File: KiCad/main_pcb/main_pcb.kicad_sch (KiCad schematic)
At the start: 5 parts

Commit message: feat(KiCad): Adds circuit for the screens
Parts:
- removed U1, U5: (no value), symbol Lily's_Pad:Logic_Converter
- added C1: (no value), symbol Lily's_Pad:Capacitor
- added J1: (no value), symbol Lily's_Pad:Header_21
- added R1: (no value), symbol Lily's_Pad:Resistor
- added S1: (no value), symbol Lily's_Pad:Push-button_Switch
- added U1: (no value), symbol Lily's_Pad:ATmega_2560
- added U5, U7: TI TXB0104DR, symbol Lily's_Pad:TI TXB0104DR
- added U8: CH340C, symbol Lily's_Pad:CH340C
- added Y1: (no value), symbol Lily's_Pad:Crystal
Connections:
- net EYE_LEFT.D/C is gone; now on net D/C: U2.3 (DC)
- net EYE_LEFT.MOSI is gone; now on net MOSI: U2.4 (MOSI)
- net EYE_LEFT.SCK is gone; now on net SCK: U2.5 (CLK)
- net EYE_RIGHT.D/C is gone; now on net D/C: U3.3 (DC)
- net EYE_RIGHT.MOSI is gone; now on net MOSI: U3.4 (MOSI)
- net EYE_RIGHT.RST_EYES is gone; now on an unnamed net: U3.1 (RST)
- net EYE_RIGHT.SCK is gone; now on net SCK: U3.5 (CLK)
- net CS_EYE_L: now also U5.4 (A3)
- net D/C: now also U4.5 (DC/RS), U1.9 (PE7), U7.10 (B4), U7.5 (A4)
- net GND: now also S1.2, U1.11 (GND), U1.32 (GND), U1.62 (GND), U1.81 (GND), U1.99 (GND), U5.7 (GND), U7.7 (GND), U8.1 (GND); no longer U4.8 (GND)
- net MOSI: now also U4.4 (MOSI), U1.21 (PB2), U7.11 (B3), U7.4 (A3)
- net RST_EYES: now also U5.5 (A4)
- net SCK: now also U4.3 (SCK), U1.20 (PB1), U7.13 (B1), U7.2 (A1)
- net VCC: now also R1.1, U1.10 (VCC), U1.100 (AVCC), U1.31 (VCC), U1.61 (VCC), U1.80 (VCC), U5.1 (V_{CCA}), U5.14 (V_{CCB}), U7.1 (V_{CCA}), U7.14 (V_{CCB}), U8.16 (VCC); no longer U4.9 (VCC)
- net MISO: now reaches U4.1 (MISO)
- net MISO: now also U1.22 (PB3), U7.12 (B2), U7.3 (A2)
- net at U4.6 (RESET): now also U5.12 (B2)
- net at U4.7 (CS): now also U5.13 (B1)
- net EYE_LEFT.CS_EYE_L: no longer names the net of U2.2 (CS)
- net EYE_LEFT.RST_EYES: no longer names the net of U2.1 (RST)
- net EYE_LEFT.RST_EYES: now also U5.10 (B4)
- net EYE_RIGHT.CS_EYE_R: no longer names the net of U3.2 (CS)
- net EYE_RIGHT.CS_EYE_R: now also U5.11 (B3)
- new net: C1.2, U8.4 (V3)
- new net: U1.34 (XTAL1), Y1.1
- new net: U1.33 (XTAL2), Y1.2
- new net CS_MAIN: U5.2 (A1)
- new net RST: R1.2, S1.1, U1.30 (~{RESET})
- new net RST_MAIN: U5.3 (A2)
- new net uC_RX: U8.2 (TXD)
- new net uC_TX: U8.3 (RXD)
- new net ~{SS}: U1.19 (PB0)
- no-connect marks 28 -> 110
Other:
- company: (none) -> Lily's Pad
- title: (none) -> Main PCB

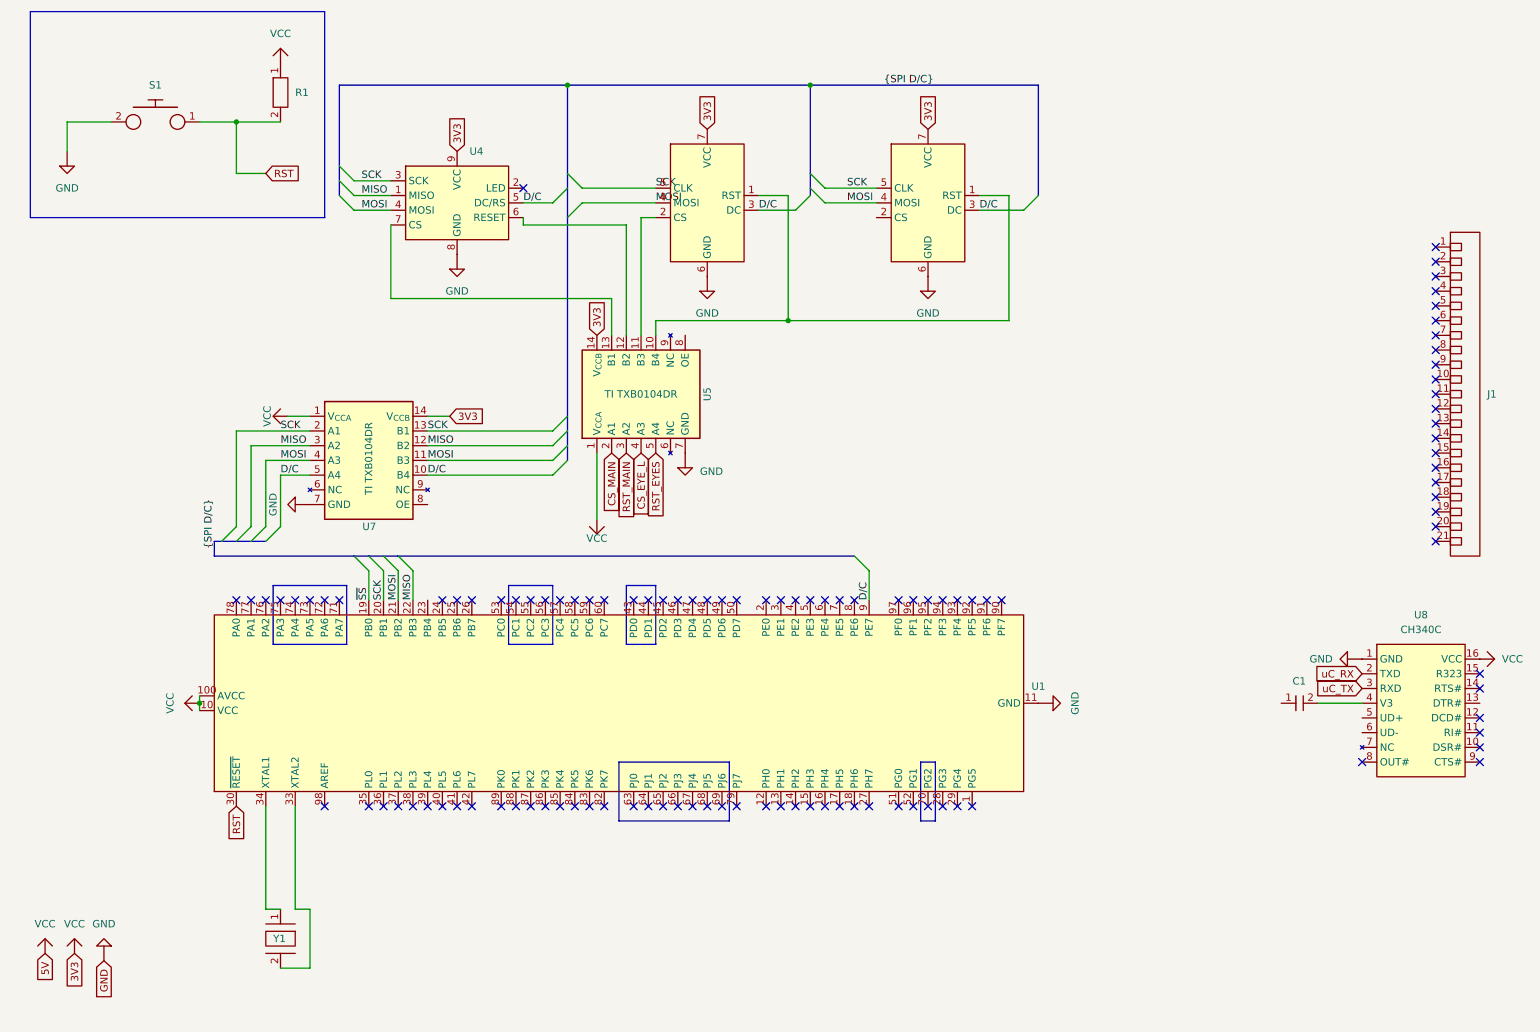
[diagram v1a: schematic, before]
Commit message: feat(KiCad): Adds partial circuit for USB to UART module
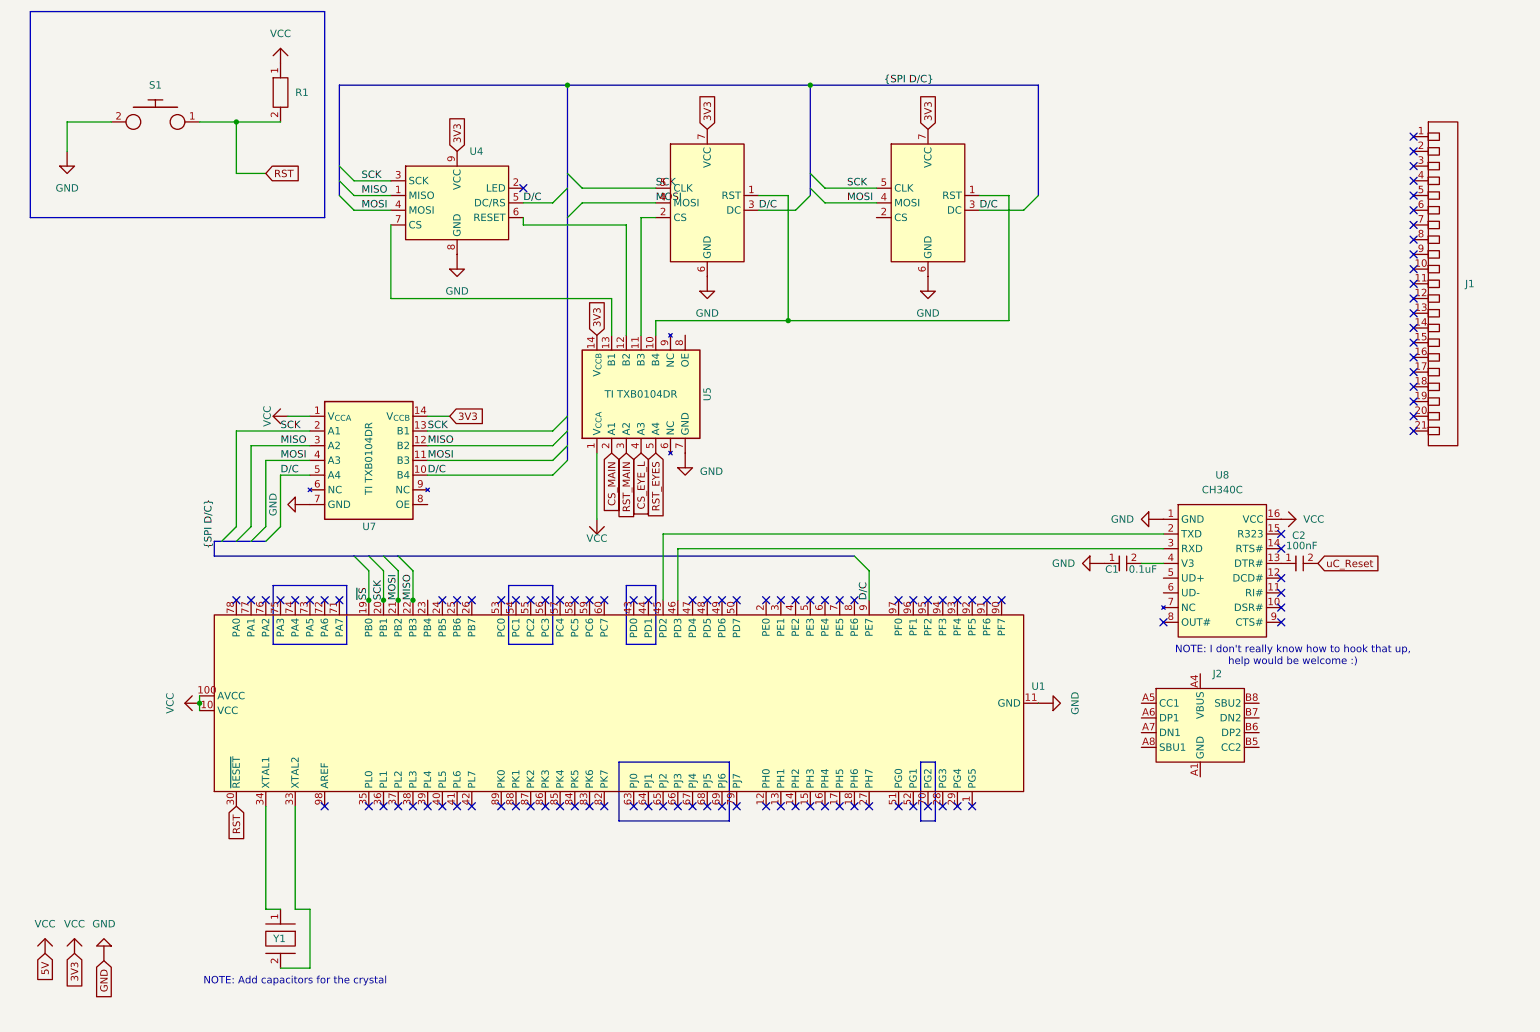
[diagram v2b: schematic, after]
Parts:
- added C2: 100nF, symbol Lily's_Pad:Capacitor
- added J2: (no value), symbol Lily's_Pad:USB_TYPE-C-31-M-14
- C1: value (none) -> 0.1uF
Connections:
- net uC_RX is gone; now on an unnamed net: U8.2 (TXD)
- net uC_TX is gone; now on an unnamed net: U8.3 (RXD)
- net GND: now also C1.1, J2.A1 (GND), J2.A12 (GND), J2.B1 (GND), J2.B12 (GND)
- net at U8.13 (DTR#): now also C2.1
- new net VBUS: J2.A4 (VBUS), J2.A9 (VBUS), J2.B4 (VBUS), J2.B9 (VBUS)
- new net uC_Reset: C2.2
- no-connect marks 110 -> 108
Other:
- note added: "NOTE: Add capacitors for the crystal"
- note added: "NOTE: I don't really know how to hook that up, help would be welcome :)"
- moved on the sheet: C1, J1, U8

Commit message: feat(KiCad): Enhances circuits, not done yet
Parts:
- added U6: TI TXB0104DR, symbol Lily's_Pad:TI TXB0104DR
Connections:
- net CS_EYE_L is gone; now on an unnamed net: U5.4 (A3)
- net CS_MAIN is gone; now on an unnamed net: U5.2 (A1)
- net RST_EYES is gone; now on an unnamed net: U5.5 (A4)
- net RST_MAIN is gone; now on an unnamed net: U5.3 (A2)
- net GND: now also U6.7 (GND)
- net VCC: now also U6.1 (V_{CCA}), U6.14 (V_{CCB})
- net at U2.2 (CS): now also U6.13 (B1)
- net at U1.13 (PH1): now also U6.2 (A1)
- no-connect marks 108 -> 109
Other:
- note added: "^ ^ JTAG DEBUGGING"
- moved on the sheet: R1, S1, U4, U5, U7

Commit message: feat(KiCad): Enhances circuits, not done yet
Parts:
- removed U4: (no value), symbol Lily's_Pad:Main_LCD_?
- added U4: SD Card Socket, symbol Lily's_Pad:SD_Card_Socket
- added U9: ILI9488, symbol Lily's_Pad:ILI9488
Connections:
- net D/C: now also U9.5 (D/C)
- net GND: now also U1.17 (PH5), U6.2 (A1), U9.2 (GND)
- net MISO: now also U4.3 (SDO), U9.9 (SDO); no longer U1.22 (PB3)
- net MOSI: now also U4.2 (SDI), U9.6 (SDI); no longer U1.21 (PB2)
- net SCK: now also U4.4 (CLK), U9.7 (SCK); no longer U1.20 (PB1)
- net VCC: now also U9.1 (VCC)
- net ~{SS}: no longer U1.19 (PB0)
- net at U2.1 (RST), U3.1 (RST): now also U6.11 (B3); no longer U5.10 (B4)
- net at U2.2 (CS): now also U6.12 (B2); no longer U6.13 (B1)
- net at U3.2 (CS): now also U6.13 (B1); no longer U5.11 (B3)
- net at U5.12 (B2): now also U9.4 (RST)
- net at U5.13 (B1): now also U9.3 (CS)
- net at U5.4 (A3): now also U1.14 (PH2); no longer U1.17 (PH5)
- net at U5.5 (A4): no longer U1.7 (PE5)
- net at U1.13 (PH1): now also U6.3 (A2); no longer U6.2 (A1)
- net at U6.4 (A3): now also U1.7 (PE5)
- new net: U4.1 (CS), U5.11 (B3)
- no-connect marks 109 -> 106
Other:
- moved on the sheet: U5, U6

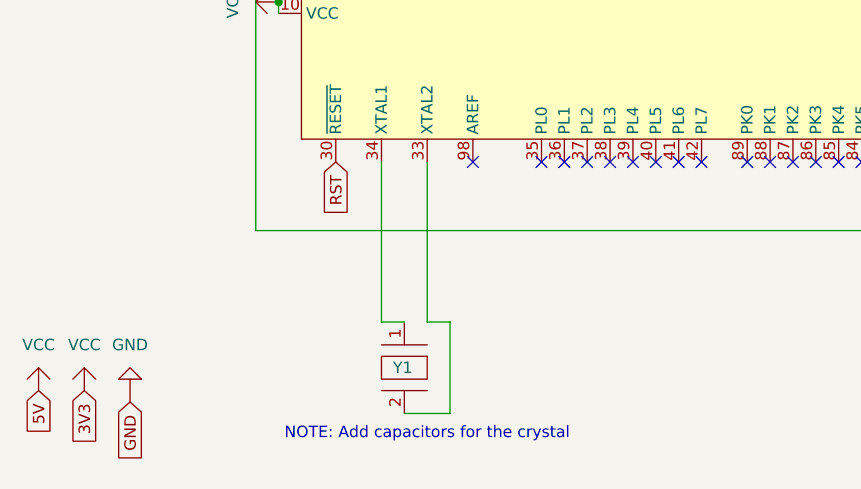
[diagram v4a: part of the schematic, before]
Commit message: feat(KiCad): Add load capacitors (2x 33pF) for the crystal
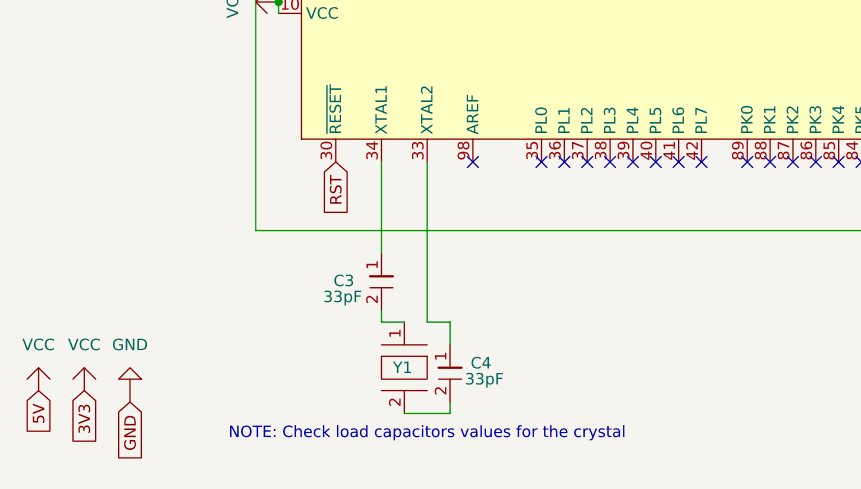
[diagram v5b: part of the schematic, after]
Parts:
- added C3, C4: 33pF, symbol Lily's_Pad:Capacitor
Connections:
- net at Y1.1: now also C3.2; no longer U1.34 (XTAL1)
- net at U1.33 (XTAL2): now also C4.1; no longer Y1.2
- new net: C4.2, Y1.2
- new net: C3.1, U1.34 (XTAL1)
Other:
- note added: "NOTE: Check load capacitors values for the crystal"
- note removed: "NOTE: Add capacitors for the crystal"
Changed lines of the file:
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@@
 		)
 	)
-	(text "NOTE: Add capacitors for the crystal"
+	(text "NOTE: Check load capacitors values for the crystal"
 		(exclude_from_sim no)
 		(at 62.23 188.976 0)
@@
 	(wire
 		(pts
+			(xy 57.15 175.26) (xy 57.15 176.53)
+		)
+		(stroke
+			(width 0)
+			(type default)
+		)
+	)
+	(wire
+		(pts
 			(xy 41.91 99.06) (xy 50.8 99.06)
 		)
@@
 	(wire
 		(pts
-			(xy 57.15 158.7499) (xy 57.15 176.53)
+			(xy 57.15 158.7499) (xy 57.15 168.91)
 		)
 		(stroke
@@
 	(wire
 		(pts
-			(xy 64.77 176.53) (xy 64.77 186.69)
+			(xy 64.77 176.53) (xy 64.77 179.07)
 		)
 		(stroke
@@
 		)
 	)
+	(wire
+		(pts
+			(xy 64.77 185.42) (xy 64.77 186.69)
+		)
+		(stroke
+			(width 0)
+			(type default)
+		)
+	)
 	(bus
 		(pts
@@
 	)
 	(symbol
+		(lib_id "Lily's_Pad:Capacitor")
+		(at 64.77 182.88 0)
+		(unit 1)
+		(body_style 1)
+		(exclude_from_sim no)
+		(in_bom yes)
+		(on_board yes)
+		(in_pos_files yes)
+		(dnp no)
+		(property "Reference" "C4"
+			(at 67.056 181.102 0)
+			(show_name no)
+			(do_not_autoplace no)
+			(effects
+				(font
+					(size 1.27 1.27)
+				)
+				(justify left)
+			)
+		)
+		(property "Value" "33pF"
+			(at 68.58 182.88 0)
+			(show_name no)
+			(do_not_autoplace no)
+			(effects
+				(font
+					(size 1.27 1.27)
+				)
+			)
+		)
+		(property "Footprint" ""
+			(at 64.77 182.88 0)
+			(hide yes)
+			(show_name no)
+			(do_not_autoplace no)
+			(effects
+				(font
+					(size 1.27 1.27)
+				)
+			)
+		)
+		(property "Datasheet" ""
+			(at 64.77 182.88 0)
+			(hide yes)
+			(show_name no)
+			(do_not_autoplace no)
+			(effects
+				(font
+					(size 1.27 1.27)
+				)
+			)
+		)
+		(property "Description" ""
+			(at 64.77 182.88 0)
+			(hide yes)
+			(show_name no)
+			(do_not_autoplace no)
+			(effects
+				(font
+					(size 1.27 1.27)
+				)
+			)
+		)
+		(pin "1"
+		)
+		(pin "2"
+		)
+		(instances
+			(project "main_pcb"
+				(path "/346fb29b-2426-4b69-9f9a-e979b6e41832"
+					(reference "C4")
+					(unit 1)
+				)
+			)
+		)
+	)
+	(symbol
 		(lib_id "Lily's_Pad:Push-button_Switch")
 		(at 222.25 43.18 270)
@@
 					(unit 1)
 				)
+			)
+		)
+	)
+	(symbol
+		(lib_id "Lily's_Pad:Capacitor")
+		(at 57.15 172.72 0)
+		(unit 1)
+		(body_style 1)
+		(exclude_from_sim no)
+		(in_bom yes)
+		(on_board yes)
+		(in_pos_files yes)
+		(dnp no)
+		(property "Reference" "C3"
+			(at 51.816 171.958 0)
+			(show_name no)
+			(do_not_autoplace no)
+			(effects
+				(font
+					(size 1.27 1.27)
+				)
+				(justify left)
+			)
+		)
+		(property "Value" "33pF"
+			(at 52.832 173.736 0)
+			(show_name no)
+			(do_not_autoplace no)
+			(effects
+				(font
+					(size 1.27 1.27)
+				)
+			)
+		)
+		(property "Footprint" ""
+			(at 57.15 172.72 0)
+			(hide yes)
+			(show_name no)
+			(do_not_autoplace no)
+			(effects
+				(font
+					(size 1.27 1.27)
+				)
+			)
+		)
+		(property "Datasheet" ""
+			(at 57.15 172.72 0)
+			(hide yes)
+			(show_name no)
+			(do_not_autoplace no)
+			(effects
+				(font
+					(size 1.27 1.27)
+				)
+			)
+		)
+		(property "Description" ""
+			(at 57.15 172.72 0)
+			(hide yes)
+			(show_name no)
+			(do_not_autoplace no)
+			(effects
+				(font
+					(size 1.27 1.27)
+				)
+			)
+		)
+		(pin "1"
+		)
+		(pin "2"
+		)
+		(instances
+			(project "main_pcb"
+				(path "/346fb29b-2426-4b69-9f9a-e979b6e41832"
+					(reference "C3")
+					(unit 1)
+				)
